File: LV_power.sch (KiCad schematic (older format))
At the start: 34 parts, among them T1 7508110151, U4 TPS76201, U5 TPS76201, U6 XCL221B18, U7 VIPER26HD

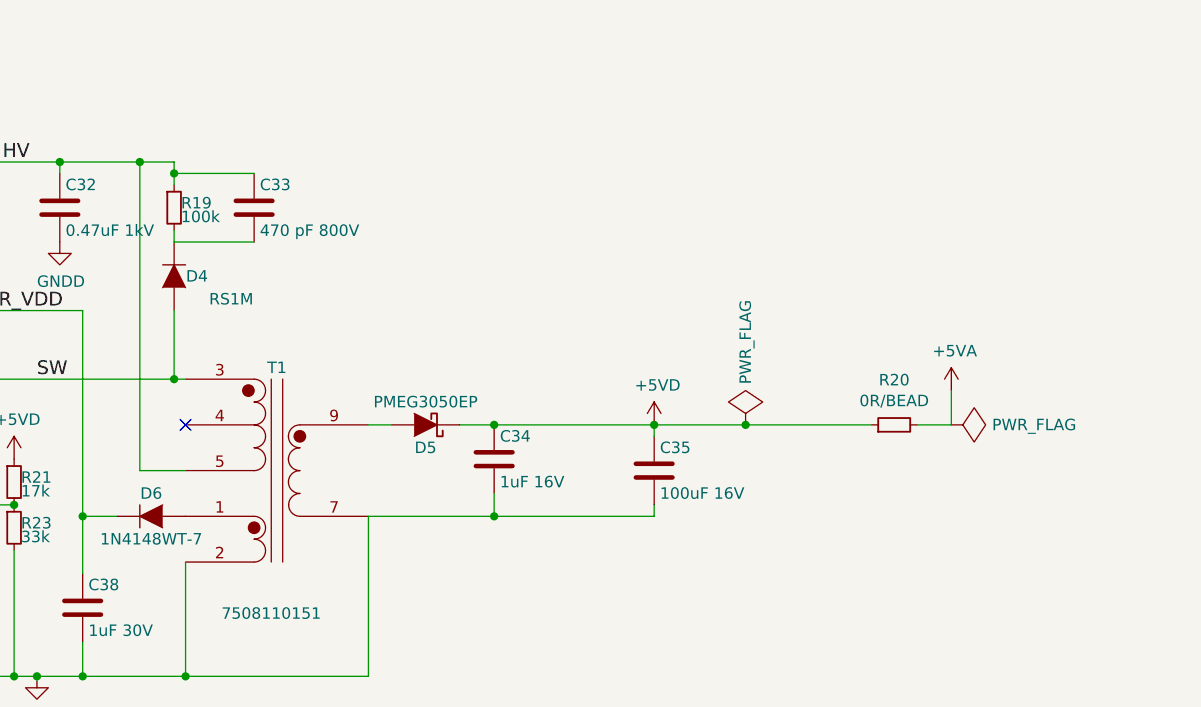
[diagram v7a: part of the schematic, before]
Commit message: stepdown PSU placed
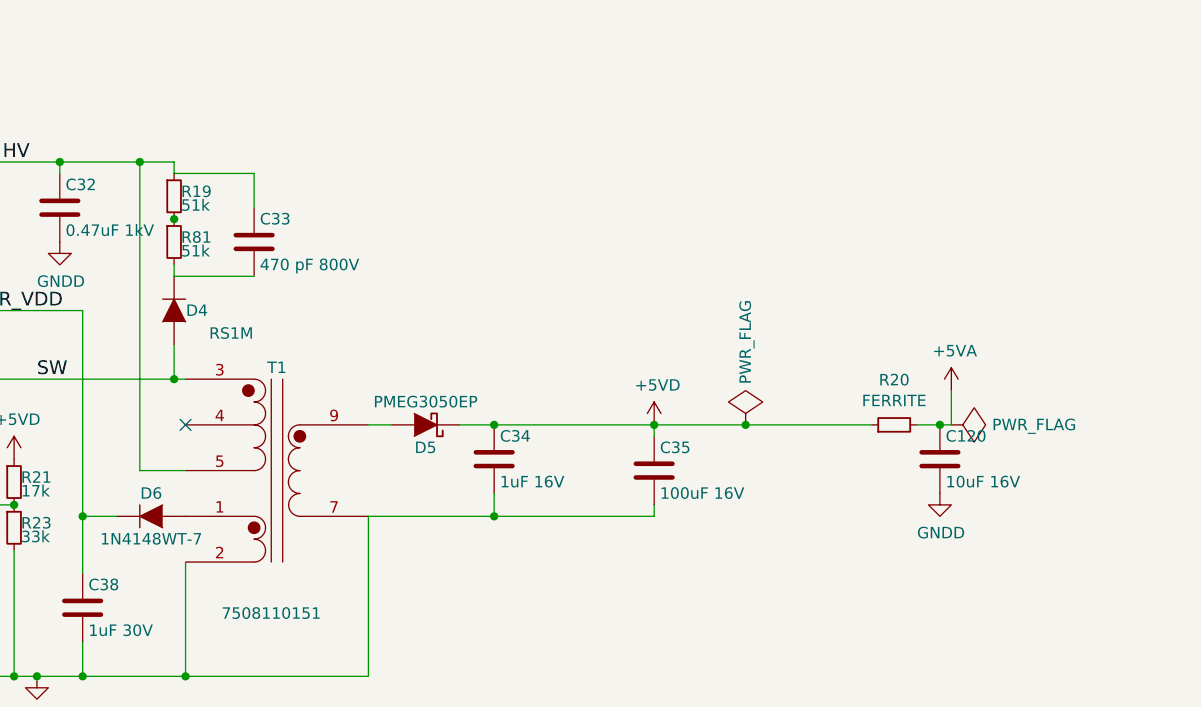
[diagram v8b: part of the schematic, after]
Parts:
- added C120: 10uF 16V, Capacitors_SMD:C_0805, symbol C
- added R81: 51k, Resistors_SMD:R_1206, symbol R_Small
- C33: footprint Capacitors_SMD:C_0805 -> Capacitors_SMD:C_1206
- R19: value 100k -> 51k; footprint Resistors_SMD:R_0805 -> Resistors_SMD:R_1206
- R20: value 0R/BEAD -> FERRITE; footprint Resistors_SMD:R_0603 -> Resistors_SMD:R_0805
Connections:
- net +5VA: now also C120.1
- net GNDD: now also C120.2
- net at C33.2, D4.1 (K): now also R81.2; no longer R19.2
- new net: R19.2, R81.1
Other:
- moved on the sheet: C33, D4
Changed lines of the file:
@@
 LIBS:TMDSCNCD28069
 LIBS:74LVC8T245
-LIBS:viper0p-etc
 LIBS:sictroller-cache
 EELAYER 25 0
@@
 $EndDescr
 $Comp
-L +5VA #PWR047
+L +5VA #PWR62
 U 1 1 57A630DE
 P 8250 4700
-F 0 "#PWR047" H 8250 4550 50  0001 C CNN
+F 0 "#PWR62" H 8250 4550 50  0001 C CNN
 F 1 "+5VA" H 8265 4873 50  0000 C CNN
 F 2 "" H 8250 4700 50  0000 C CNN
@@
 P 8000 4850
 F 0 "R20" V 8196 4850 50  0000 C CNN
-F 1 "0R/BEAD" V 8105 4850 50  0000 C CNN
-F 2 "Resistors_SMD:R_0603" H 8000 4850 50  0001 C CNN
+F 1 "FERRITE" V 8105 4850 50  0000 C CNN
+F 2 "Resistors_SMD:R_0805" H 8000 4850 50  0001 C CNN
 F 3 "" H 8000 4850 50  0000 C CNN
 	1    8000 4850
@@
 $EndComp
 $Comp
-L GNDD #PWR048
+L GNDD #PWR63
 U 1 1 57A63878
 P 8550 1600
-F 0 "#PWR048" H 8550 1350 50  0001 C CNN
+F 0 "#PWR63" H 8550 1350 50  0001 C CNN
 F 1 "GNDD" H 8555 1427 50  0000 C CNN
 F 2 "" H 8550 1600 50  0000 C CNN
@@
 $EndComp
 $Comp
-L +3.3V #PWR049
+L +3.3V #PWR64
 U 1 1 57A63913
 P 9350 800
-F 0 "#PWR049" H 9350 650 50  0001 C CNN
+F 0 "#PWR64" H 9350 650 50  0001 C CNN
 F 1 "+3.3V" H 9365 973 50  0000 C CNN
 F 2 "" H 9350 800 50  0000 C CNN
@@
 $EndComp
 $Comp
-L PWR_FLAG #FLG050
+L PWR_FLAG #FLG4
 U 1 1 57A8371C
 P 8250 4850
-F 0 "#FLG050" H 8250 4945 50  0001 C CNN
+F 0 "#FLG4" H 8250 4945 50  0001 C CNN
 F 1 "PWR_FLAG" V 8250 5028 50  0000 L CNN
 F 2 "" H 8250 4850 50  0000 C CNN
@@
 $EndComp
 $Comp
-L +3.3VA #PWR051
+L +3.3VA #PWR58
 U 1 1 57F8E4FA
 P 6500 800
-F 0 "#PWR051" H 6500 650 50  0001 C CNN
+F 0 "#PWR58" H 6500 650 50  0001 C CNN
 F 1 "+3.3VA" H 6500 940 50  0000 C CNN
 F 2 "" H 6500 800 50  0000 C CNN
@@
 $EndComp
 $Comp
-L GNDD #PWR052
+L GNDD #PWR50
 U 1 1 57FAEA88
 P 3800 1050
-F 0 "#PWR052" H 3800 800 50  0001 C CNN
+F 0 "#PWR50" H 3800 800 50  0001 C CNN
 F 1 "GNDD" H 3805 877 50  0000 C CNN
 F 2 "" H 3800 1050 50  0000 C CNN
@@
 $EndComp
 $Comp
-L GNDD #PWR053
+L GNDD #PWR48
 U 1 1 57FAEAB4
 P 2600 1050
-F 0 "#PWR053" H 2600 800 50  0001 C CNN
+F 0 "#PWR48" H 2600 800 50  0001 C CNN
 F 1 "GNDD" H 2605 877 50  0000 C CNN
 F 2 "" H 2600 1050 50  0000 C CNN
@@
 $EndComp
 $Comp
-L +1V8 #PWR054
+L +1V8 #PWR51
 U 1 1 57FAFE13
 P 4150 1150
-F 0 "#PWR054" H 4150 1000 50  0001 C CNN
+F 0 "#PWR51" H 4150 1000 50  0001 C CNN
 F 1 "+1V8" H 4150 1290 50  0000 C CNN
 F 2 "" H 4150 1150 50  0000 C CNN
@@
 $EndComp
 $Comp
-L GNDD #PWR055
+L GNDD #PWR52
 U 1 1 57FAFE97
 P 4150 1350
-F 0 "#PWR055" H 4150 1100 50  0001 C CNN
+F 0 "#PWR52" H 4150 1100 50  0001 C CNN
 F 1 "GNDD" H 4155 1177 50  0000 C CNN
 F 2 "" H 4150 1350 50  0000 C CNN
@@
 $EndComp
 $Comp
-L GNDD #PWR056
+L GNDD #PWR47
 U 1 1 57FAFF6A
 P 1900 1150
-F 0 "#PWR056" H 1900 900 50  0001 C CNN
+F 0 "#PWR47" H 1900 900 50  0001 C CNN
 F 1 "GNDD" H 1905 977 50  0000 C CNN
 F 2 "" H 1900 1150 50  0000 C CNN
@@
 $EndComp
 $Comp
-L +5VD #PWR057
+L +5VD #PWR46
 U 1 1 57FB04EE
 P 1900 900
-F 0 "#PWR057" H 1900 750 50  0001 C CNN
+F 0 "#PWR46" H 1900 750 50  0001 C CNN
 F 1 "+5VD" H 1915 1073 50  0000 C CNN
 F 2 "" H 1900 900 50  0000 C CNN
@@
 $EndComp
 $Comp
-L +5VD #PWR058
+L +5VD #PWR60
 U 1 1 57FB15F5
 P 7900 800
-F 0 "#PWR058" H 7900 650 50  0001 C CNN
+F 0 "#PWR60" H 7900 650 50  0001 C CNN
 F 1 "+5VD" H 7915 973 50  0000 C CNN
 F 2 "" H 7900 800 50  0000 C CNN
@@
 $EndComp
 $Comp
-L GNDD #PWR059
+L GNDD #PWR57
 U 1 1 57FB234D
 P 5700 1600
-F 0 "#PWR059" H 5700 1350 50  0001 C CNN
+F 0 "#PWR57" H 5700 1350 50  0001 C CNN
 F 1 "GNDD" H 5705 1427 50  0000 C CNN
 F 2 "" H 5700 1600 50  0000 C CNN
@@
 $EndComp
 $Comp
-L +5VD #PWR060
+L +5VD #PWR56
 U 1 1 57FB236B
 P 5050 800
-F 0 "#PWR060" H 5050 650 50  0001 C CNN
+F 0 "#PWR56" H 5050 650 50  0001 C CNN
 F 1 "+5VD" H 5065 973 50  0000 C CNN
 F 2 "" H 5050 800 50  0000 C CNN
@@
 $EndComp
 $Comp
-L +5VD #PWR061
+L +5VD #PWR59
 U 1 1 57FB262C
 P 6950 4850
-F 0 "#PWR061" H 6950 4700 50  0001 C CNN
+F 0 "#PWR59" H 6950 4700 50  0001 C CNN
 F 1 "+5VD" H 6965 5023 50  0000 C CNN
 F 2 "" H 6950 4850 50  0000 C CNN
@@
 $EndComp
 $Comp
-L GNDD #PWR062
+L GNDD #PWR54
 U 1 1 57FB554E
 P 4250 5950
-F 0 "#PWR062" H 4250 5700 50  0001 C CNN
+F 0 "#PWR54" H 4250 5700 50  0001 C CNN
 F 1 "GNDD" H 4255 5777 50  0000 C CNN
 F 2 "" H 4250 5950 50  0000 C CNN
@@
 $EndComp
 $Comp
-L GNDD #PWR063
+L GNDD #PWR55
 U 1 1 57FB7D48
 P 4350 4050
-F 0 "#PWR063" H 4350 3800 50  0001 C CNN
+F 0 "#PWR55" H 4350 3800 50  0001 C CNN
 F 1 "GNDD" H 4355 3877 50  0000 C CNN
 F 2 "" H 4350 4050 50  0000 C CNN
@@
 L D D4
 U 1 1 57FB81B6
-P 4850 4200
-F 0 "D4" V 4850 4300 50  0000 C CNN
-F 1 "RS1M" V 4950 4450 50  0000 C CNN
-F 2 "Diodes_SMD:SMA_Standard" H 4850 4200 50  0001 C CNN
-F 3 "" H 4850 4200 50  0000 C CNN
-	1    4850 4200
+P 4850 4350
+F 0 "D4" V 4850 4450 50  0000 C CNN
+F 1 "RS1M" V 4950 4600 50  0000 C CNN
+F 2 "Diodes_SMD:SMA_Standard" H 4850 4350 50  0001 C CNN
+F 3 "" H 4850 4350 50  0000 C CNN
+	1    4850 4350
 	0    1    1    0
 $EndComp
@@
 L C C33
 U 1 1 57FB85E4
-P 5200 3900
-F 0 "C33" H 5225 4000 50  0000 L CNN
-F 1 "470 pF 800V" H 5225 3800 50  0000 L CNN
-F 2 "Capacitors_SMD:C_0805" H 5238 3750 50  0001 C CNN
-F 3 "" H 5200 3900 50  0000 C CNN
-	1    5200 3900
-	1    0    0    -1
-$EndComp
-$Comp
-L R_Small R19
-U 1 1 57FB87D2
-P 4850 3900
-F 0 "R19" H 4880 3920 50  0000 L CNN
-F 1 "100k" H 4880 3860 50  0000 L CNN
-F 2 "Resistors_SMD:R_0805" H 4850 3900 50  0001 C CNN
-F 3 "" H 4850 3900 50  0000 C CNN
-	1    4850 3900
+P 5200 4050
+F 0 "C33" H 5225 4150 50  0000 L CNN
+F 1 "470 pF 800V" H 5225 3950 50  0000 L CNN
+F 2 "Capacitors_SMD:C_1206" H 5238 3900 50  0001 C CNN
+F 3 "" H 5200 4050 50  0000 C CNN
+	1    5200 4050
 	1    0    0    -1
 $EndComp
@@
 $EndComp
 $Comp
-L +5VD #PWR064
+L +5VD #PWR53
 U 1 1 57FBA909
 P 4150 5000
-F 0 "#PWR064" H 4150 4850 50  0001 C CNN
+F 0 "#PWR53" H 4150 4850 50  0001 C CNN
 F 1 "+5VD" H 4165 5173 50  0000 C CNN
 F 2 "" H 4150 5000 50  0000 C CNN
@@
 $EndComp
 $Comp
-L PWR_FLAG #FLG065
+L PWR_FLAG #FLG3
 U 1 1 57FBE4C9
 P 7350 4850
-F 0 "#FLG065" H 7350 4945 50  0001 C CNN
+F 0 "#FLG3" H 7350 4945 50  0001 C CNN
 F 1 "PWR_FLAG" V 7350 5028 50  0000 L CNN
 F 2 "" H 7350 4850 50  0000 C CNN
@@
 $EndComp
 $Comp
-L GNDD #PWR066
+L GNDD #PWR49
 U 1 1 57FCE56A
 P 2600 4350
-F 0 "#PWR066" H 2600 4100 50  0001 C CNN
+F 0 "#PWR49" H 2600 4100 50  0001 C CNN
 F 1 "GNDD" H 2600 4200 50  0000 C CNN
 F 2 "" H 2600 4350 50  0000 C CNN
@@
 $EndComp
 $Comp
-L PWR_FLAG #FLG067
+L PWR_FLAG #FLG2
 U 1 1 57FCEFC8
 P 2700 4350
-F 0 "#FLG067" H 2700 4445 50  0001 C CNN
+F 0 "#FLG2" H 2700 4445 50  0001 C CNN
 F 1 "PWR_FLAG" V 2700 4528 50  0000 L CNN
 F 2 "" H 2700 4350 50  0000 C CNN
@@
 	4700 5050 4700 3700
 Wire Wire Line
-	3450 3700 4850 3700
-Wire Wire Line
 	2300 5950 5700 5950
 Wire Wire Line
@@
 Connection ~ 4850 4650
 Wire Wire Line
-	5200 4050 4850 4050
-Wire Wire Line
-	4850 4050 4850 4000
-Wire Wire Line
-	4850 3700 4850 3800
+	5200 4200 4850 4200
+Wire Wire Line
+	4850 4200 4850 4150
 Connection ~ 4700 3700
-Wire Wire Line
-	5200 3750 4850 3750
-Connection ~ 4850 3750
 Connection ~ 4150 5200
 Wire Wire Line
@@
 	2700 4350 2600 4350
 Wire Wire Line
-	4850 4350 4850 4650
+	4850 4500 4850 4650
 Text Label 4250 4650 0    60   ~ 0
 SW
@@
 Wire Wire Line
 	2300 4550 3250 4550
+$Comp
+L R_Small R81
+U 1 1 57F9585B
+P 4850 4050
+F 0 "R81" H 4880 4070 50  0000 L CNN
+F 1 "51k" H 4880 4010 50  0000 L CNN
+F 2 "Resistors_SMD:R_1206" H 4850 4050 50  0001 C CNN
+F 3 "" H 4850 4050 50  0000 C CNN
+	1    4850 4050
+	1    0    0    -1
+$EndComp
+Wire Wire Line
+	3450 3700 4850 3700
+$Comp
+L R_Small R19
+U 1 1 57F9614D
+P 4850 3850
+F 0 "R19" H 4880 3870 50  0000 L CNN
+F 1 "51k" H 4880 3810 50  0000 L CNN
+F 2 "Resistors_SMD:R_1206" H 4850 3850 50  0001 C CNN
+F 3 "" H 4850 3850 50  0000 C CNN
+	1    4850 3850
+	1    0    0    -1
+$EndComp
+Wire Wire Line
+	4850 3750 5200 3750
+Wire Wire Line
+	5200 3750 5200 3900
+Wire Wire Line
+	4850 3700 4850 3750
+Connection ~ 4850 3950
+$Comp
+L C C120
+U 1 1 57F987E3
+P 8200 5000
+F 0 "C120" H 8225 5100 50  0000 L CNN
+F 1 "10uF 16V" H 8225 4900 50  0000 L CNN
+F 2 "Capacitors_SMD:C_0805" H 8238 4850 50  0001 C CNN
+F 3 "" H 8200 5000 50  0000 C CNN
+	1    8200 5000
+	1    0    0    -1
+$EndComp
+$Comp
+L GNDD #PWR61
+U 1 1 57F99976
+P 8200 5150
+F 0 "#PWR61" H 8200 4900 50  0001 C CNN
+F 1 "GNDD" H 8205 4977 50  0000 C CNN
+F 2 "" H 8200 5150 50  0000 C CNN
+F 3 "" H 8200 5150 50  0000 C CNN
+	1    8200 5150
+	1    0    0    -1
+$EndComp
+Connection ~ 8200 4850
 $EndSCHEMATC
